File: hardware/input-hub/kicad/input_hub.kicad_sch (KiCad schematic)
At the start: 46 parts, among them J1 ACJMIH, J10 Conn_01x01_Pin, J11 S2B-PH-SM4-TB_LF__SN_, J2 ACJMIH, J3 ACJMIH, J4 ACJMIH, J5 8P8C, J6 BM04B-SRSS-TB_LF__SN_, J7 Conn_01x04, J8 Conn_01x02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

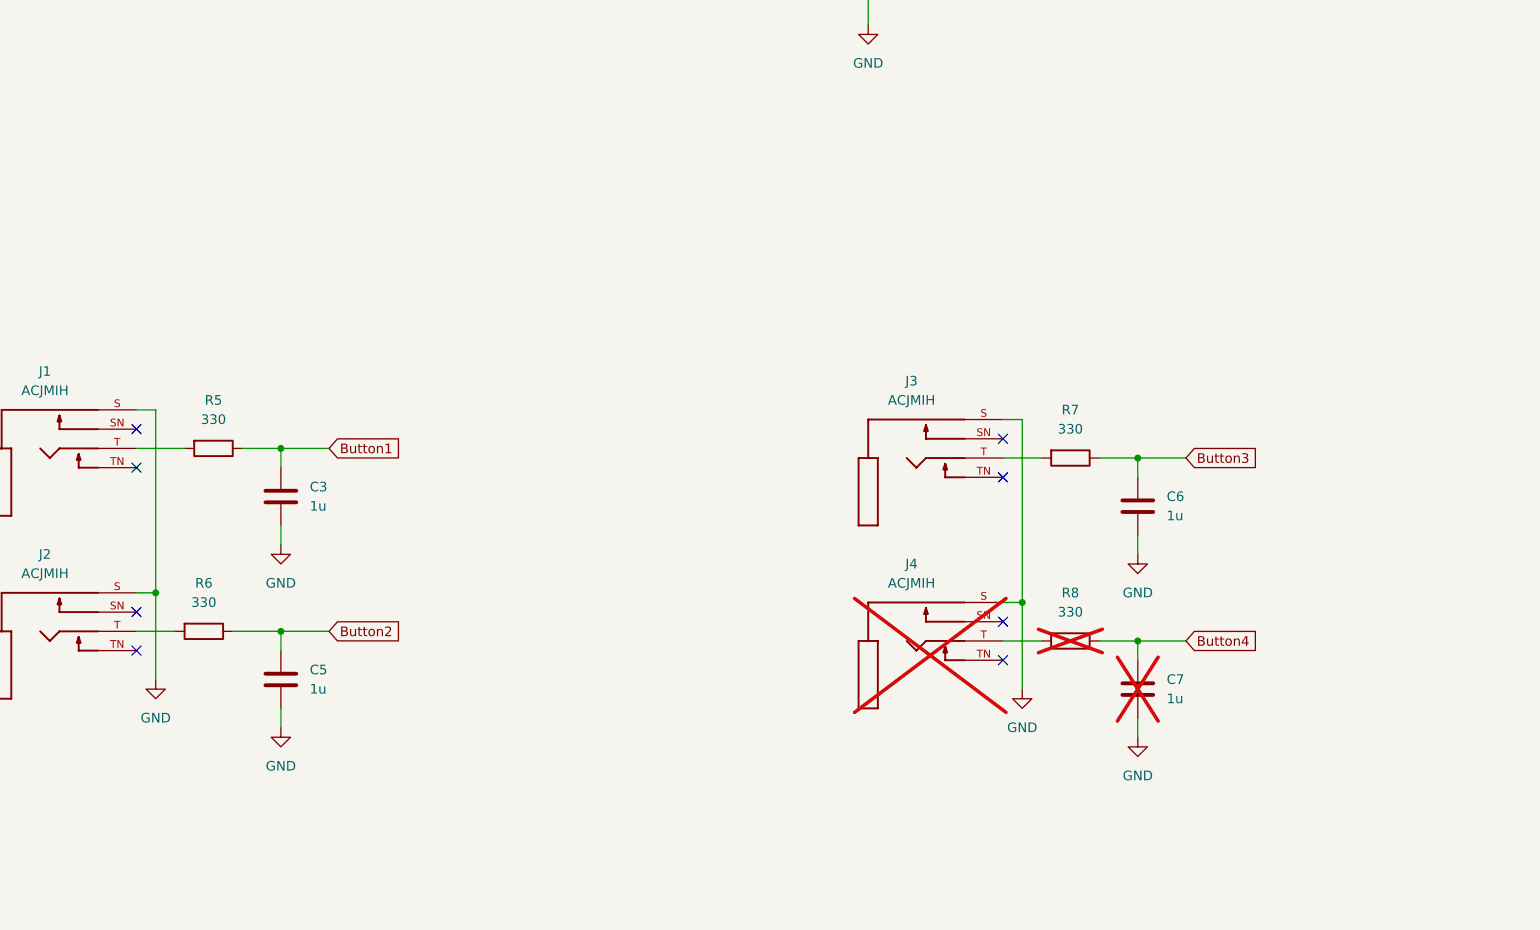
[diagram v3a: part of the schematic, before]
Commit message: feat: add PJ-307 alternate pedal jacks
- Import the HOOYA PJ-307/C2939173 symbol, footprint, and STEP model.
  - Replace the stale SJ1-3523N library assets with the PJ-307 part.
  - Add 3.5 mm alternate pedal jack footprints under the 1/4 in pedal jacks.
  - Update silkscreen labels and artwork
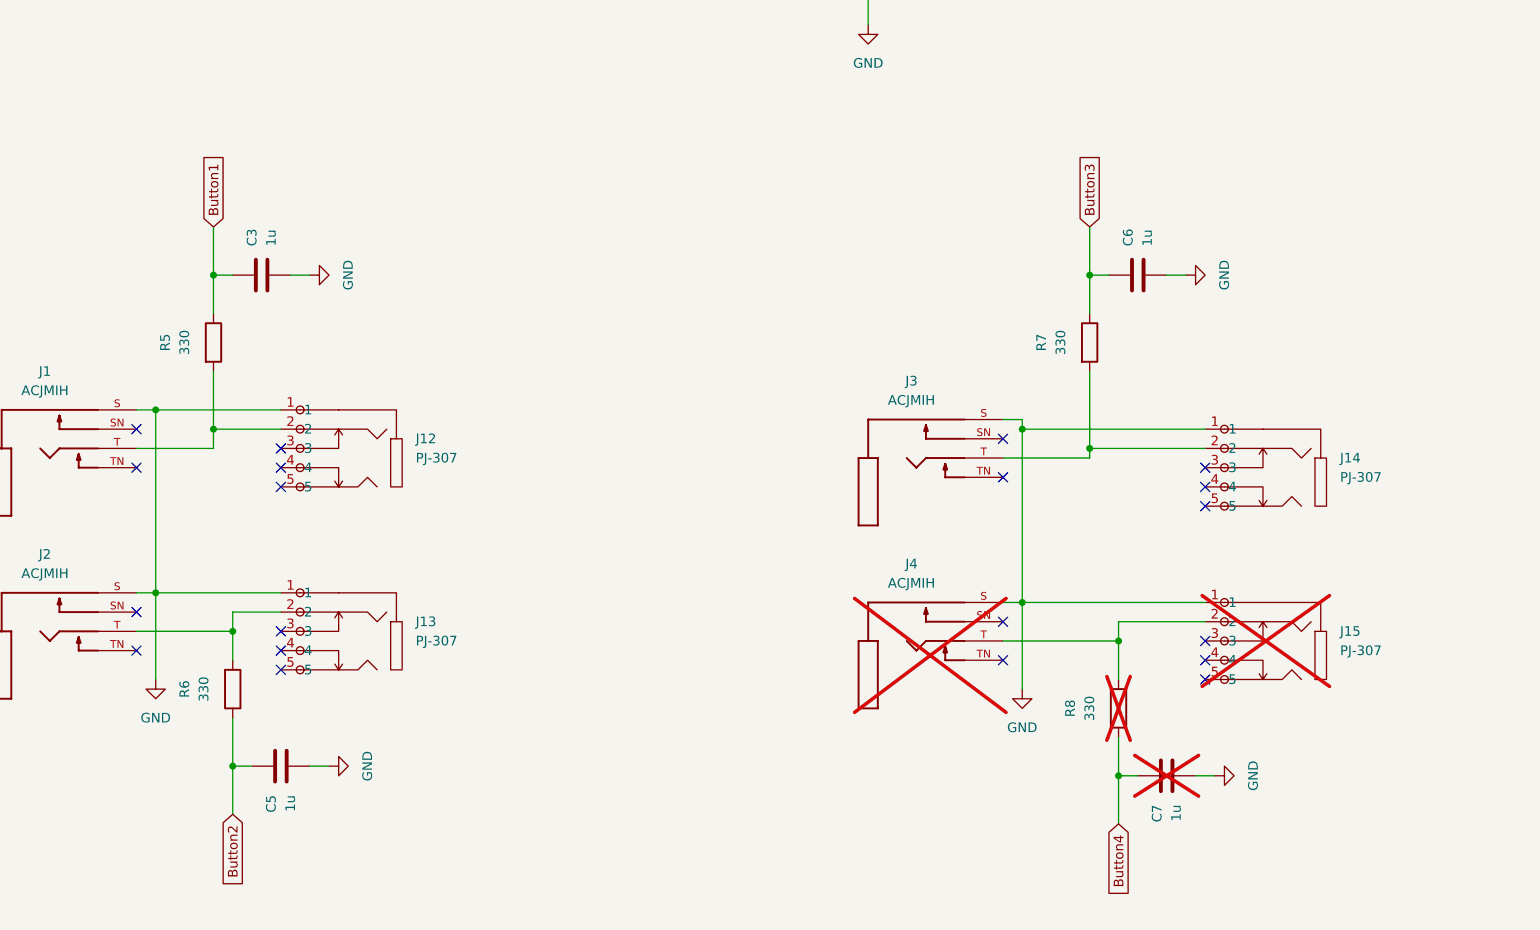
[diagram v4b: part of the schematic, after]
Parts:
- added J12, J13, J14, J15: PJ-307, input_hub:AUDIO-TH_PJ-307, symbol 3.5mm:PJ-307_C2939173
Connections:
- net GND: now also J12.1, J13.1, J14.1, J15.1
- net at J3.T, R7.2: now also J14.2
- net at J2.T, R6.2: now also J13.2
- net at J1.T, R5.2: now also J12.2
- net at J4.T, R8.2: now also J15.2
- no-connect marks 21 -> 33
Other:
- moved on the sheet: C3, C5, C6, C7, R5, R6, R7, R8

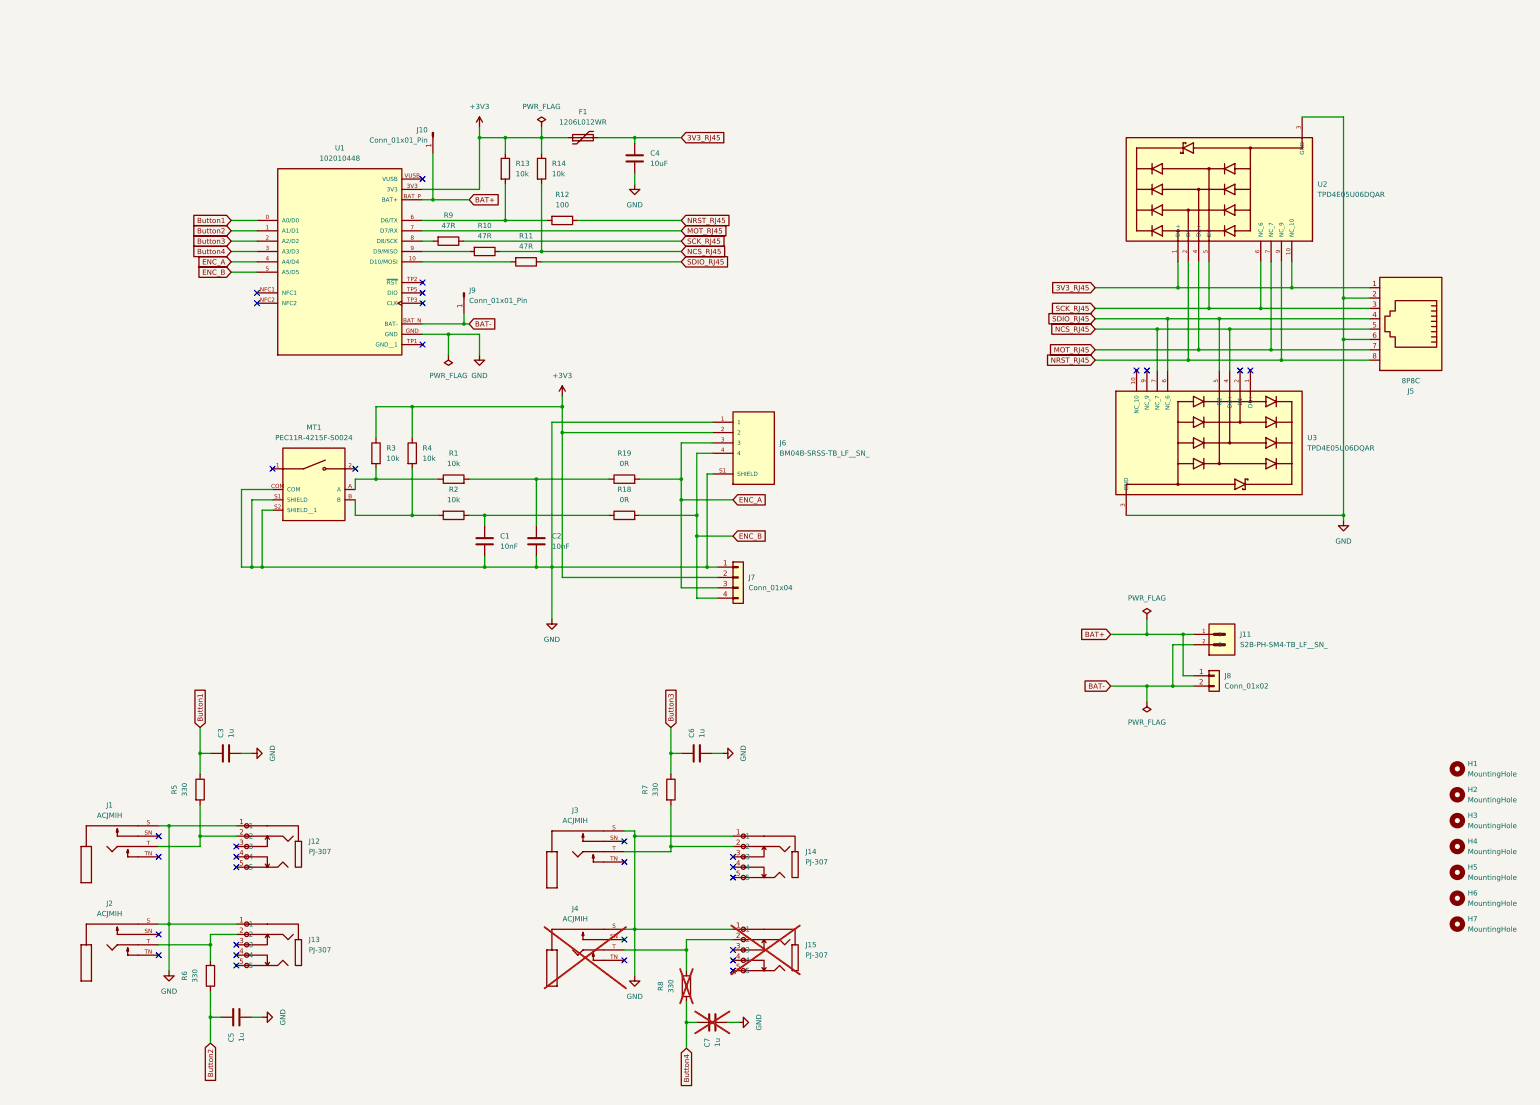
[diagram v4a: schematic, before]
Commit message: feat: remove input hub EC11 encoder and update 3D models
- Remove the EC11 encoder and supporting debounce network from the input hub.
  - Add project-local 3D model links for imported input hub footprints.
  - Vendor the RJ45 footprint with the exact Amphenol 54602-908LF model.
  - Add the XIAO battery solder access symbol and footprint.
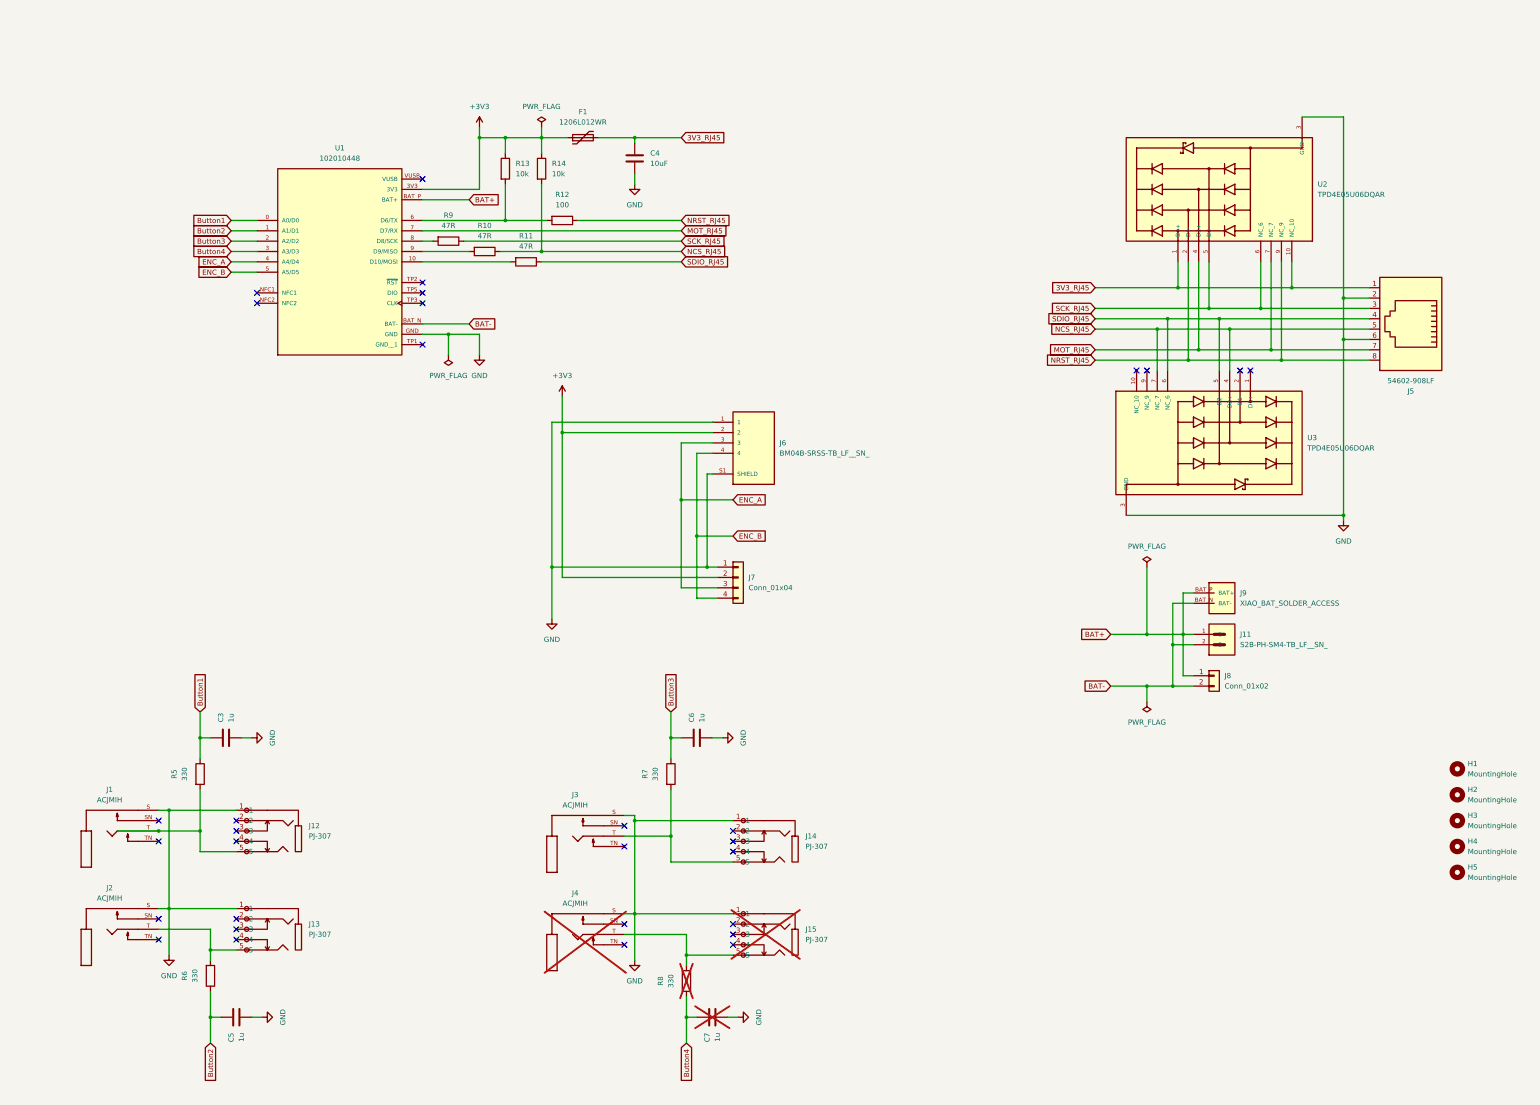
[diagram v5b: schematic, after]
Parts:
- removed C1, C2: 10nF, Capacitor_SMD:C_0603_1608Metric, symbol Device:C
- removed H6, H7: MountingHole, MountingHole:MountingHole_3.2mm_M3_ISO14580, symbol Mechanical:MountingHole
- removed J10, J9: Conn_01x01_Pin, Connector_Pin:Pin_D0.7mm_L6.5mm_W1.8mm_FlatFork, symbol Connector:Conn_01x01_Pin
- removed MT1: PEC11R-4215F-S0024, input_hub:XDCR_PEC11R-4215F-S0024, symbol PEC11R:PEC11R-4215F-S0024
- removed R1, R2, R3, R4: 10k, Resistor_SMD:R_0603_1608Metric, symbol Device:R
- removed R18, R19: 0R, Resistor_SMD:R_0603_1608Metric, symbol Device:R
- added J9: XIAO_BAT_SOLDER_ACCESS, input_hub:XIAO_BAT_SOLDER_ACCESS, symbol XIAO_BAT:XIAO_BAT_SOLDER_ACCESS
- J5: value 8P8C -> 54602-908LF; footprint Connector_RJ:RJ45_Amphenol_54602-x08_Horizontal -> input_hub:RJ45_Amphenol_54602-x08_Horizontal; 3D Model Source (none) -> https://cdn.amphenol-cs.com/media/wysiwyg/files/3d/s54602-9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; Digi-Key MFR. Part # (none) -> 54602-908LF; Digi-Key Part # (none) -> 609-1046-ND; Digi-Key URL (none) -> https://www.digikey.com/en/products/detail/amphenol-cs-fci/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; MFR. Part # (none) -> 54602-908LF; Manufacturer (none) -> Amphenol ICC (FCI); Manufacturer URL (none) -> https://www.amphenol-cs.com/product/54602908lf.html; TraceParts URL (none) -> https://www.traceparts.com/en/product/rs-components-ampheno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
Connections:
- net BAT+: now also J9.BAT_P (BAT+)
- net BAT-: now also J9.BAT_N (BAT-)
- net at J1.T, R5.2: now also J12.5; no longer J12.2
- net at J3.T, R7.2: now also J14.5; no longer J14.2
- net at J2.T, R6.2: now also J13.5; no longer J13.2
- net at J4.T, R8.2: now also J15.5; no longer J15.2
- no-connect marks 33 -> 31
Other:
- moved on the sheet: C3, C6, C7, J1, J12, J13, J14, J15, J2, J3, J4, R5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

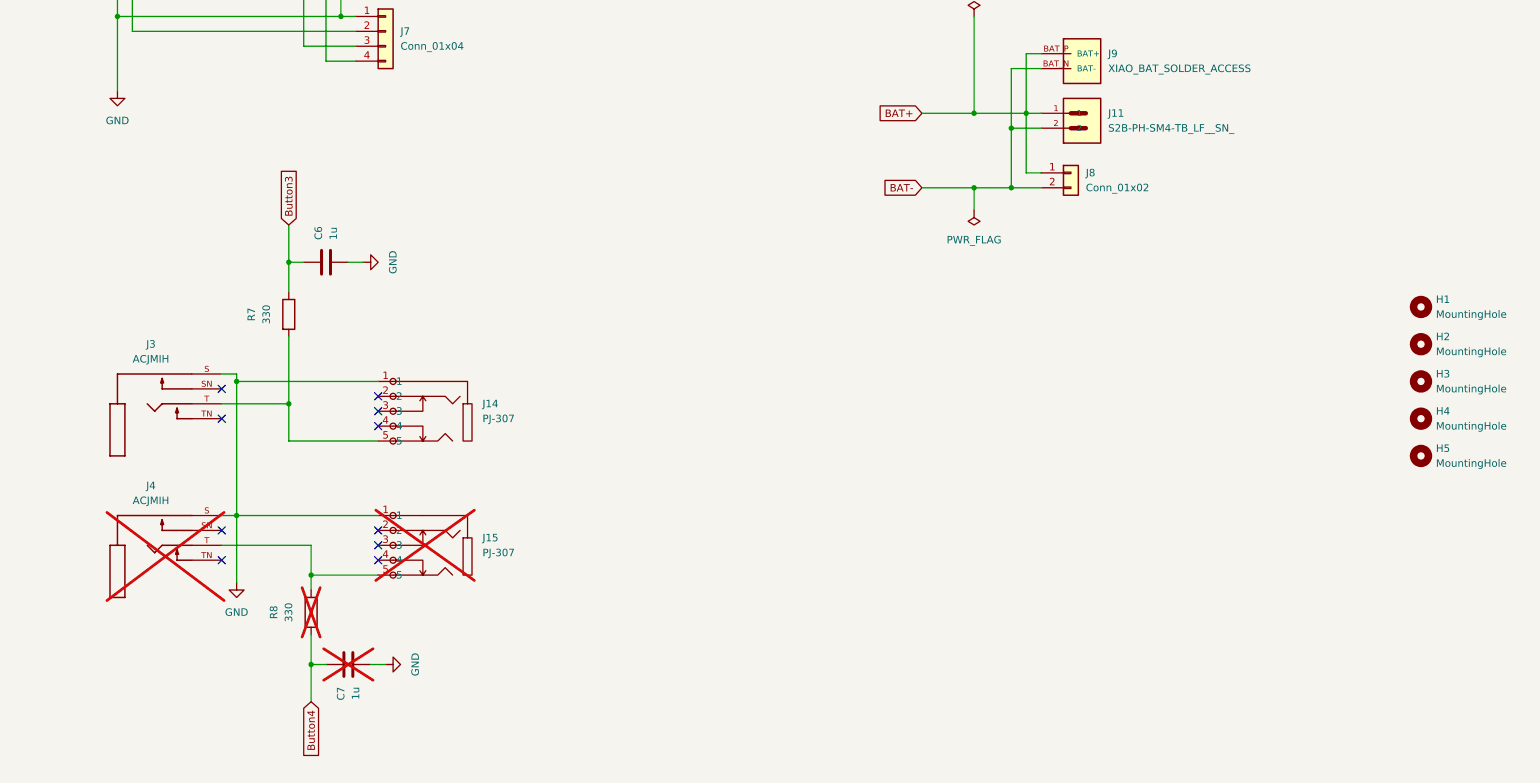
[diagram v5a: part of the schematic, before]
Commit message: feat: remove third TS jack and make vertical JST battery connector
- Remove the third pedal jack option to reduce board width.
  - Align edge connectors for a cleaner enclosure-facing layout.
  - Replace the horizontal battery JST with a vertical B2B-PH-SM4-TB footprint.
  - Remove stale horizontal JST symbol, footprint, and model assets.
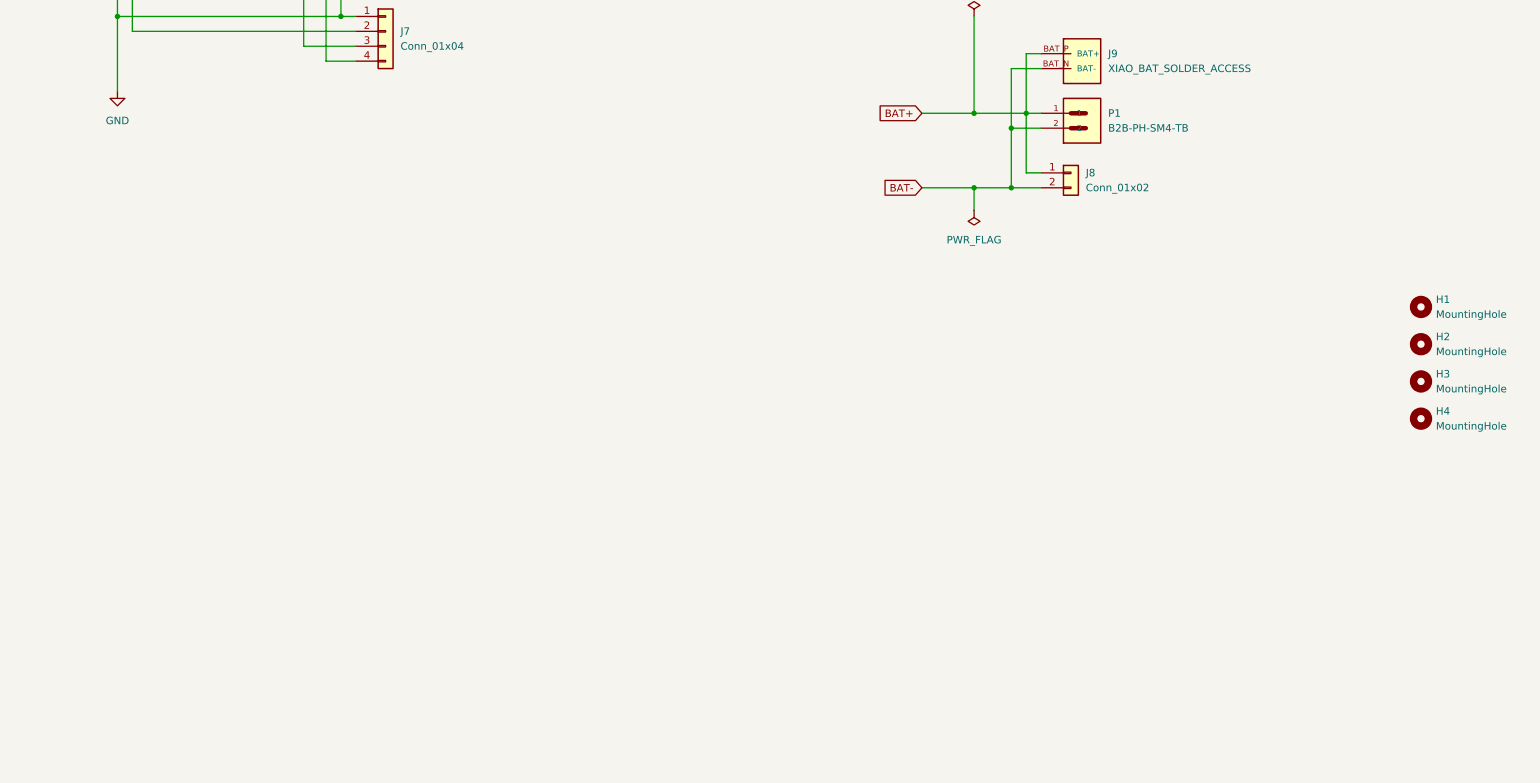
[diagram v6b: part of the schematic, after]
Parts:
- removed C6, C7: 1u, Capacitor_SMD:C_0603_1608Metric, symbol Device:C
- removed H5: MountingHole, MountingHole:MountingHole_3.2mm_M3_ISO14580, symbol Mechanical:MountingHole
- removed J11: S2B-PH-SM4-TB_LF__SN_, input_hub:JST_S2B-PH-SM4-TB_LF__SN_, symbol BAT:S2B-PH-SM4-TB_LF__SN_
- removed J14, J15: PJ-307, input_hub:AUDIO-TH_PJ-307, symbol 3.5mm:PJ-307_C2939173
- removed J3, J4: ACJMIH, input_hub:AMPHENOL_ACJMIH, symbol ACJMIH:ACJMIH
- removed R7, R8: 330, Resistor_SMD:R_0603_1608Metric, symbol Device:R
- added P1: B2B-PH-SM4-TB, input_hub:JST_PH_B2B-PH-SM4-TB_1x02-1MP_P2.00mm_Vertical, symbol BAT:B2B-PH-SM4-TB
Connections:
- net BAT+: now also P1.1
- net BAT-: now also P1.2
- no-connect marks 31 -> 21
